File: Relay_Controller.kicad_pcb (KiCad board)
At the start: 2 copper layers, 45.5 x 62 mm, 9 parts, among them J1 AC_MOTOR, J2 SWITCH_5V, J3 AC_220V, K1 RELAY_SRD_C

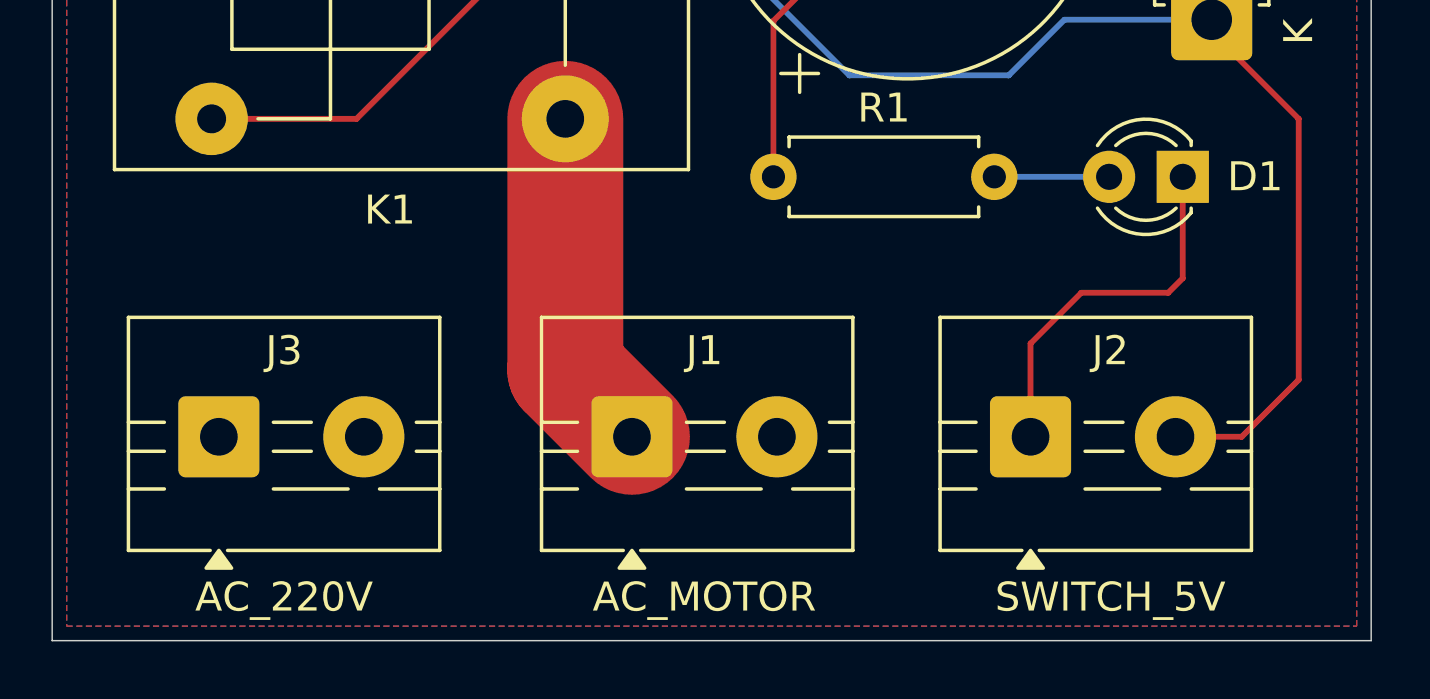
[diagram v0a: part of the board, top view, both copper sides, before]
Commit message: fix: use parallel line -> relay/led
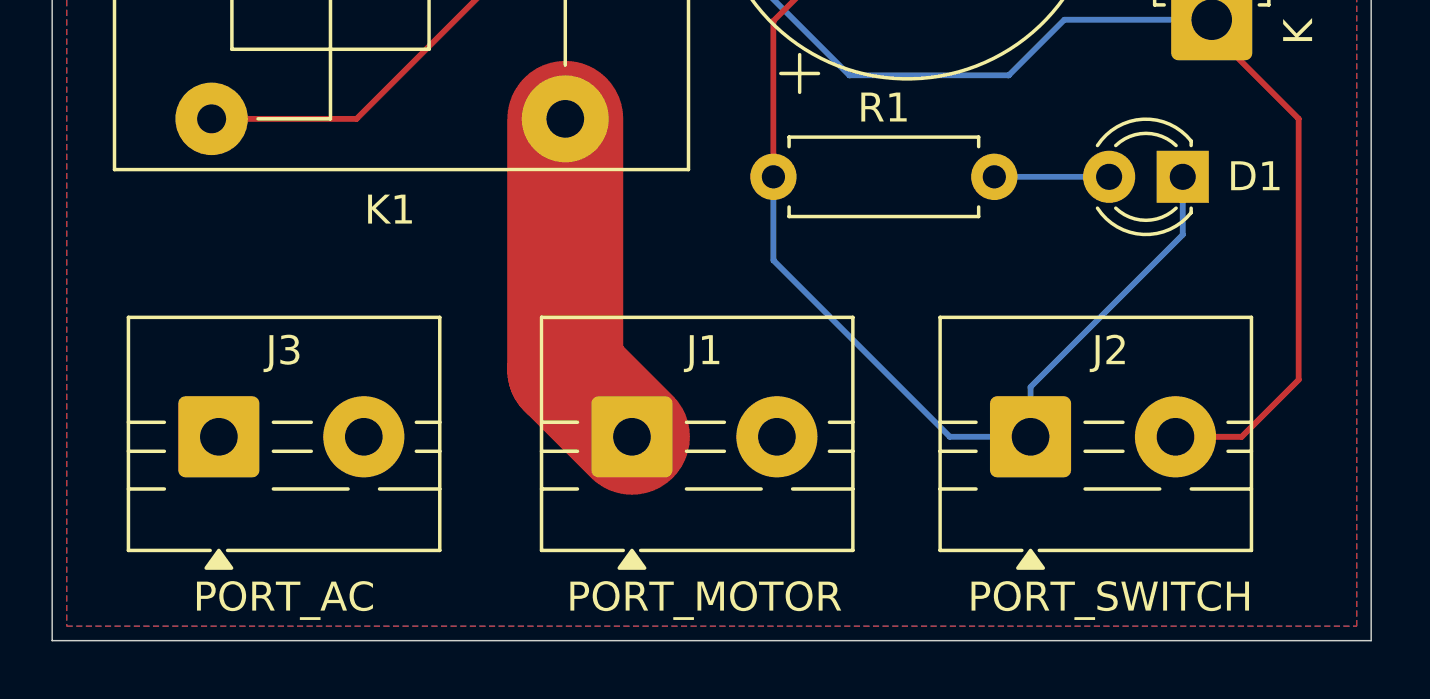
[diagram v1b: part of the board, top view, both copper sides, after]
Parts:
- J1: value AC_MOTOR -> PORT_MOTOR
- J2: value SWITCH_5V -> PORT_SWITCH
- J3: value AC_220V -> PORT_AC
- K1: value RELAY_SRD_C -> SANYOU_SRD_Form_C
- R1: value 470 -> 470 Ohm
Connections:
- C1 pad 1: Net-(PS1-+Vout) -> V3
- PS1 pad 4: Net-(PS1-+Vout) -> V3
- R1 pad 1: Net-(PS1-+Vout) -> V3
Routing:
- net V3: track 12.9 -> 59.3 mm
- net Net-(PS1-+Vout): track 33.9 -> 0.00 mm
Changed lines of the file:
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@@
 	(net 0 "")
 	(net 1 "Net-(D2-A)")
-	(net 2 "Net-(PS1-+Vout)")
-	(net 3 "V4")
-	(net 4 "V2")
-	(net 5 "unconnected-(K1-Pad4)")
-	(net 6 "V5")
-	(net 7 "V1")
-	(net 8 "Net-(D1-A)")
-	(net 9 "V3")
+	(net 2 "V4")
+	(net 3 "V2")
+	(net 4 "unconnected-(K1-Pad4)")
+	(net 5 "V5")
+	(net 6 "V1")
+	(net 7 "Net-(D1-A)")
+	(net 8 "V3")
 	(footprint "TerminalBlock:TerminalBlock_MaiXu_MX126-5.0-02P_1x02_P5.00mm"
 		(layer "F.Cu")
@@
 			)
 		)
-		(property "Value" "AC_MOTOR"
+		(property "Value" "PORT_MOTOR"
 			(at 2.5 5.5325 0)
 			(layer "F.SilkS")
@@
 			(remove_unused_layers no)
 			(roundrect_rratio 0.089286)
-			(net 6 "V5")
+			(net 5 "V5")
 			(pinfunction "Pin_1")
 			(pintype "passive")
@@
 			(layers "*.Cu" "*.Mask")
 			(remove_unused_layers no)
-			(net 7 "V1")
+			(net 6 "V1")
 			(pinfunction "Pin_2")
 			(pintype "passive")
@@
 			(layers "*.Cu" "*.Mask")
 			(remove_unused_layers no)
-			(net 7 "V1")
+			(net 6 "V1")
 			(pinfunction "AC/L")
 			(pintype "power_in")
@@
 			(layers "*.Cu" "*.Mask")
 			(remove_unused_layers no)
-			(net 4 "V2")
+			(net 3 "V2")
 			(pinfunction "AC/N")
 			(pintype "power_in")
@@
 			(layers "*.Cu" "*.Mask")
 			(remove_unused_layers no)
-			(net 2 "Net-(PS1-+Vout)")
+			(net 8 "V3")
 			(pinfunction "+Vout")
 			(pintype "power_out")
@@
 			(remove_unused_layers no)
 			(roundrect_rratio 0.089286)
-			(net 3 "V4")
+			(net 2 "V4")
 			(pinfunction "K")
 			(pintype "passive")
@@
 			(remove_unused_layers no)
 			(roundrect_rratio 0.104167)
-			(net 2 "Net-(PS1-+Vout)")
+			(net 8 "V3")
 			(pintype "passive")
 		)
@@
 			)
 		)
-		(property "Value" "SWITCH_5V"
+		(property "Value" "PORT_SWITCH"
 			(at 2.75 5.5325 0)
 			(layer "F.SilkS")
@@
 			(remove_unused_layers no)
 			(roundrect_rratio 0.089286)
-			(net 9 "V3")
+			(net 8 "V3")
 			(pinfunction "Pin_1")
 			(pintype "passive")
@@
 			(layers "*.Cu" "*.Mask")
 			(remove_unused_layers no)
-			(net 3 "V4")
+			(net 2 "V4")
 			(pinfunction "Pin_2")
 			(pintype "passive")
@@
 			(layers "*.Cu" "*.Mask")
 			(remove_unused_layers no)
-			(net 9 "V3")
+			(net 8 "V3")
 			(pinfunction "K")
 			(pintype "passive")
@@
 			(layers "*.Cu" "*.Mask")
 			(remove_unused_layers no)
-			(net 8 "Net-(D1-A)")
+			(net 7 "Net-(D1-A)")
 			(pinfunction "A")
 			(pintype "passive")
@@
 			)
 		)
-		(property "Value" "AC_220V"
+		(property "Value" "PORT_AC"
 			(at 2.25 5.5325 0)
 			(layer "F.SilkS")
@@
 			(remove_unused_layers no)
 			(roundrect_rratio 0.089286)
-			(net 7 "V1")
+			(net 6 "V1")
 			(pinfunction "Pin_1")
 			(pintype "passive")
@@
 			(layers "*.Cu" "*.Mask")
 			(remove_unused_layers no)
-			(net 4 "V2")
+			(net 3 "V2")
 			(pinfunction "Pin_2")
 			(pintype "passive")
@@
 			)
 		)
-		(property "Value" "RELAY_SRD_C"
+		(property "Value" "SANYOU_SRD_Form_C"
 			(at 7.65 -8.95 0)
 			(layer "F.Fab")
@@
 			(layers "*.Cu" "*.Mask")
 			(remove_unused_layers no)
-			(net 4 "V2")
+			(net 3 "V2")
 			(pintype "passive")
 		)
@@
 			(layers "*.Cu" "*.Mask")
 			(remove_unused_layers no)
-			(net 6 "V5")
+			(net 5 "V5")
 			(pintype "passive")
 		)
@@
 			(layers "*.Cu" "*.Mask")
 			(remove_unused_layers no)
-			(net 5 "unconnected-(K1-Pad4)")
+			(net 4 "unconnected-(K1-Pad4)")
 			(pintype "passive+no_connect")
 		)
@@
 			(layers "*.Cu" "*.Mask")
 			(remove_unused_layers no)
-			(net 3 "V4")
+			(net 2 "V4")
 			(pintype "passive")
 		)
@@
 			)
 		)
-		(property "Value" "470"
+		(property "Value" "470 Ohm"
 			(at 3.81 2.37 0)
 			(layer "F.Fab")
@@
 			(layers "*.Cu" "*.Mask")
 			(remove_unused_layers no)
-			(net 2 "Net-(PS1-+Vout)")
+			(net 8 "V3")
 			(pintype "passive")
 		)
@@
 			(layers "*.Cu" "*.Mask")
 			(remove_unused_layers no)
-			(net 8 "Net-(D1-A)")
+			(net 7 "Net-(D1-A)")
 			(pintype "passive")
 		)
@@
 	)
 	(segment
-		(start 160.88 103.12)
-		(end 160.88 108.5)
-		(width 0.2)
-		(layer "F.Cu")
-		(net 2)
-	)
-	(segment
-		(start 163 101)
-		(end 160.88 103.12)
-		(width 0.2)
-		(layer "F.Cu")
-		(net 2)
-	)
-	(segment
-		(start 165.5 101)
-		(end 163 101)
-		(width 0.2)
-		(layer "F.Cu")
-		(net 2)
-	)
-	(segment
-		(start 169.5 101)
-		(end 171 99.5)
-		(width 0.2)
-		(layer "B.Cu")
-		(net 2)
-	)
-	(segment
-		(start 171 99.5)
-		(end 171 88)
-		(width 0.2)
-		(layer "B.Cu")
-		(net 2)
-	)
-	(segment
-		(start 171 88)
-		(end 172.705 86.295)
-		(width 0.2)
-		(layer "B.Cu")
-		(net 2)
-	)
-	(segment
-		(start 172.705 86.295)
-		(end 175.675 86.295)
-		(width 0.2)
-		(layer "B.Cu")
-		(net 2)
-	)
-	(segment
-		(start 165.5 101)
-		(end 169.5 101)
-		(width 0.2)
-		(layer "B.Cu")
-		(net 2)
-	)
-	(segment
 		(start 176 103.5)
 		(end 179 106.5)
 		(width 0.2)
 		(layer "F.Cu")
-		(net 3)
+		(net 2)
 	)
 	(segment
@@
 		(width 0.2)
 		(layer "F.Cu")
-		(net 3)
+		(net 2)
 	)
 	(segment
@@
 		(width 0.2)
 		(layer "F.Cu")
-		(net 3)
+		(net 2)
 	)
 	(segment
@@
 		(width 0.2)
 		(layer "F.Cu")
-		(net 3)
+		(net 2)
 	)
 	(segment
@@
 		(width 0.2)
 		(layer "F.Cu")
-		(net 3)
+		(net 2)
 	)
 	(segment
@@
 		(width 0.2)
 		(layer "B.Cu")
-		(net 3)
+		(net 2)
 	)
 	(segment
@@
 		(width 0.2)
 		(layer "B.Cu")
-		(net 3)
+		(net 2)
 	)
 	(segment
@@
 		(width 0.2)
 		(layer "B.Cu")
-		(net 3)
+		(net 2)
 	)
 	(segment
@@
 		(width 0.2)
 		(layer "B.Cu")
-		(net 3)
+		(net 2)
 	)
 	(segment
@@
 		(width 0.2)
 		(layer "B.Cu")
-		(net 3)
+		(net 2)
 	)
 	(segment
@@
 		(width 0.2)
 		(layer "B.Cu")
-		(net 3)
+		(net 2)
 	)
 	(segment
@@
 		(width 0.2)
 		(layer "F.Cu")
-		(net 4)
+		(net 3)
 	)
 	(segment
@@
 		(width 4)
 		(layer "F.Cu")
-		(net 6)
+		(net 5)
 	)
 	(segment
@@
 		(width 4)
 		(layer "F.Cu")
-		(net 6)
+		(net 5)
 	)
 	(segment
@@
 		(width 0.2)
 		(layer "B.Cu")
-		(net 8)
+		(net 7)
 	)
 	(segment
-		(start 169.75 114.25)
-		(end 171.5 112.5)
+		(start 160.88 103.12)
+		(end 160.88 108.5)
 		(width 0.2)
 		(layer "F.Cu")
-		(net 9)
+		(net 8)
 	)
 	(segment
-		(start 171.5 112.5)
-		(end 174.5 112.5)
+		(start 163 101)
+		(end 160.88 103.12)
 		(width 0.2)
 		(layer "F.Cu")
-		(net 9)
+		(net 8)
 	)
 	(segment
-		(start 175 112)
-		(end 175 108.5)
+		(start 165.5 101)
+		(end 163 101)
 		(width 0.2)
 		(layer "F.Cu")
-		(net 9)
+		(net 8)
 	)
 	(segment
-		(start 174.5 112.5)
-		(end 175 112)
+		(start 169.5 101)
+		(end 171 99.5)
 		(width 0.2)
-		(layer "F.Cu")
-		(net 9)
+		(layer "B.Cu")
+		(net 8)
+	)
+	(segment
+		(start 171 99.5)
+		(end 171 88)
+		(width 0.2)
+		(layer "B.Cu")
+		(net 8)
+	)
+	(segment
+		(start 171 88)
+		(end 172.705 86.295)
+		(width 0.2)
+		(layer "B.Cu")
+		(net 8)
+	)
+	(segment
+		(start 172.705 86.295)
+		(end 175.675 86.295)
+		(width 0.2)
+		(layer "B.Cu")
+		(net 8)
+	)
+	(segment
+		(start 175 110.5)
+		(end 169.75 115.75)
+		(width 0.2)
+		(layer "B.Cu")
+		(net 8)
+	)
+	(segment
+		(start 160.88 111.38)
+		(end 160.88 108.5)
+		(width 0.2)
+		(layer "B.Cu")
+		(net 8)
+	)
+	(segment
+		(start 169.75 115.75)
+		(end 169.75 117.4675)
+		(width 0.2)
+		(layer "B.Cu")
+		(net 8)
+	)
+	(segment
+		(start 175 108.5)
+		(end 175 110.5)
+		(width 0.2)
+		(layer "B.Cu")
+		(net 8)
+	)
+	(segment
+		(start 166.9675 117.4675)
+		(end 160.88 111.38)
+		(width 0.2)
+		(layer "B.Cu")
+		(net 8)
 	)
 	(segment
 		(start 169.75 117.4675)
-		(end 169.75 114.25)
+		(end 166.9675 117.4675)
 		(width 0.2)
-		(layer "F.Cu")
-		(net 9)
+		(layer "B.Cu")
+		(net 8)
+	)
+	(segment
+		(start 165.5 101)
+		(end 169.5 101)
+		(width 0.2)
+		(layer "B.Cu")
+		(net 8)
 	)
 	(zone
-		(net 7)
+		(net 6)
 		(net_name "V1")
 		(layer "F.Cu")
@@
 	)
 	(zone
-		(net 4)
+		(net 3)
 		(net_name "V2")
 		(layer "B.Cu")

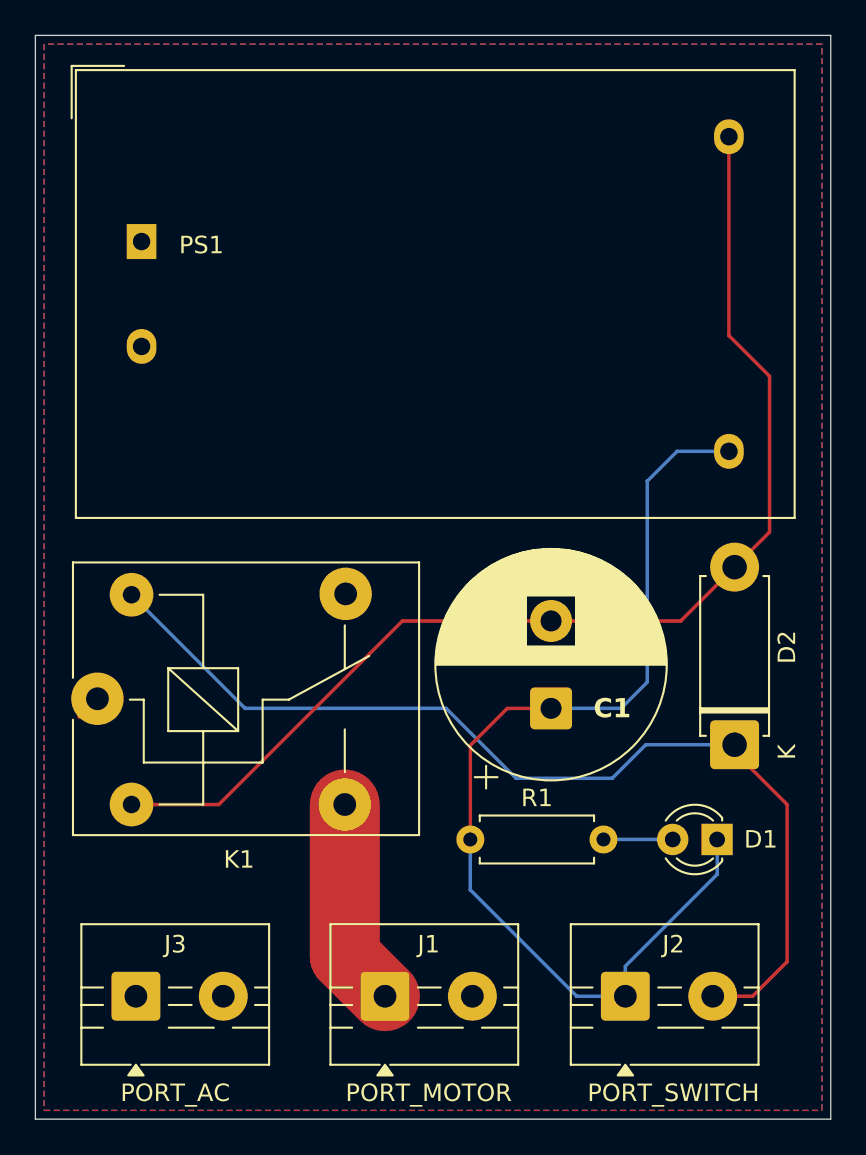
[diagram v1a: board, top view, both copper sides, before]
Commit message: Fix: +R=100 -> ensure LED turn on.
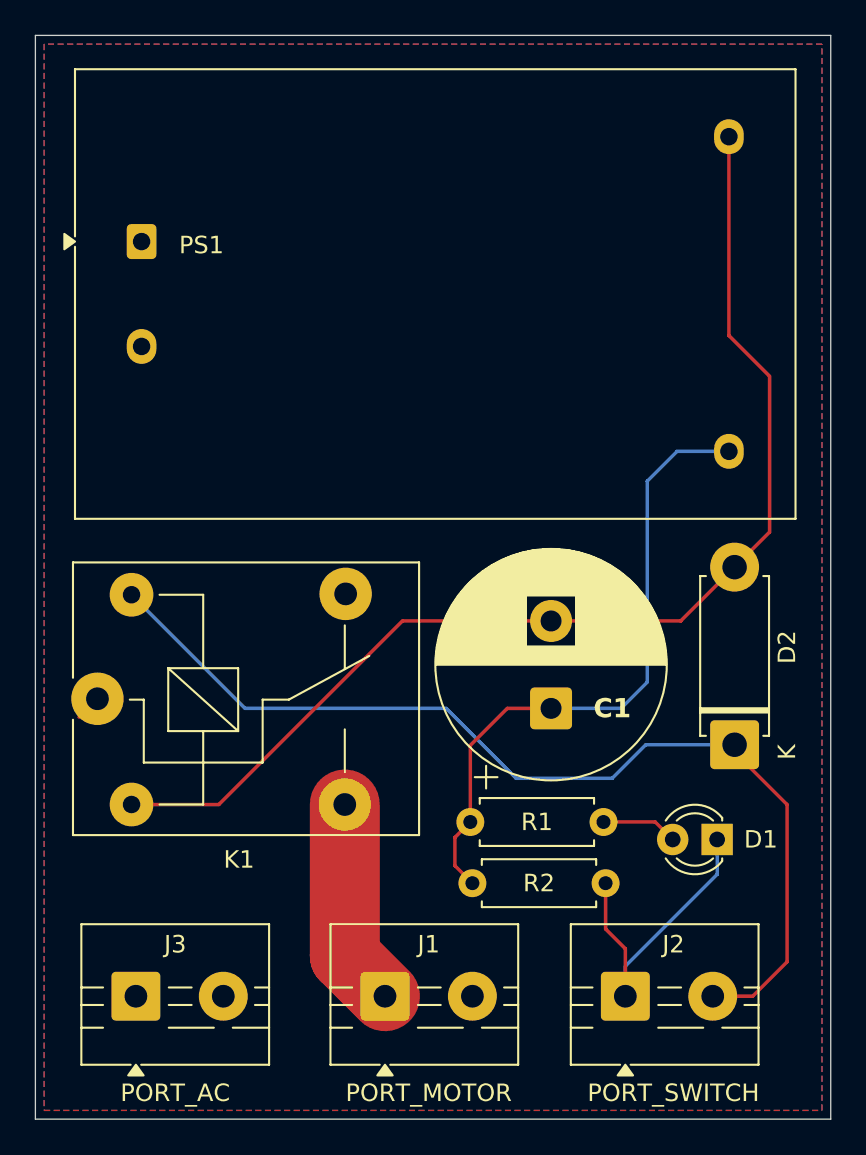
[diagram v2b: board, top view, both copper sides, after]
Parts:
- added R2: 100, Resistor_THT:R_Axial_DIN0207_L6.3mm_D2.5mm_P7.62mm_Horizontal, F.Cu at (161.0, 111.0)
- moved R1 1.00 mm to (160.9, 107.5)
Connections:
- C1 pad 1: V3 -> Net-(PS1-+Vout)
- PS1 pad 4: V3 -> Net-(PS1-+Vout)
- R1 pad 1: V3 -> Net-(PS1-+Vout)
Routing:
- net V3: track 59.3 -> 19.7 mm
- net Net-(PS1-+Vout): track 0.00 -> 37.3 mm
